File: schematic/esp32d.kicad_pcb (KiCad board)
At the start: 2 copper layers, 86.4 x 50.8 mm, 47 parts, among them IC1 CP2102N-A01-GQFN28R, J1 USB_B_Micro, J2 Conn_02x08_Odd_Even, J3 Conn_02x08_Odd_Even, J4 Conn_01x02, Q1 SS8050-G, Q2 SS8050-G, Q3 DMG2307L-7, SW1 SW_Push, U1 AMS1117-3.3, U2 ESP32-WROOM-32D, U3 DizzyBITLogo, U4 MCP73831-2-OT

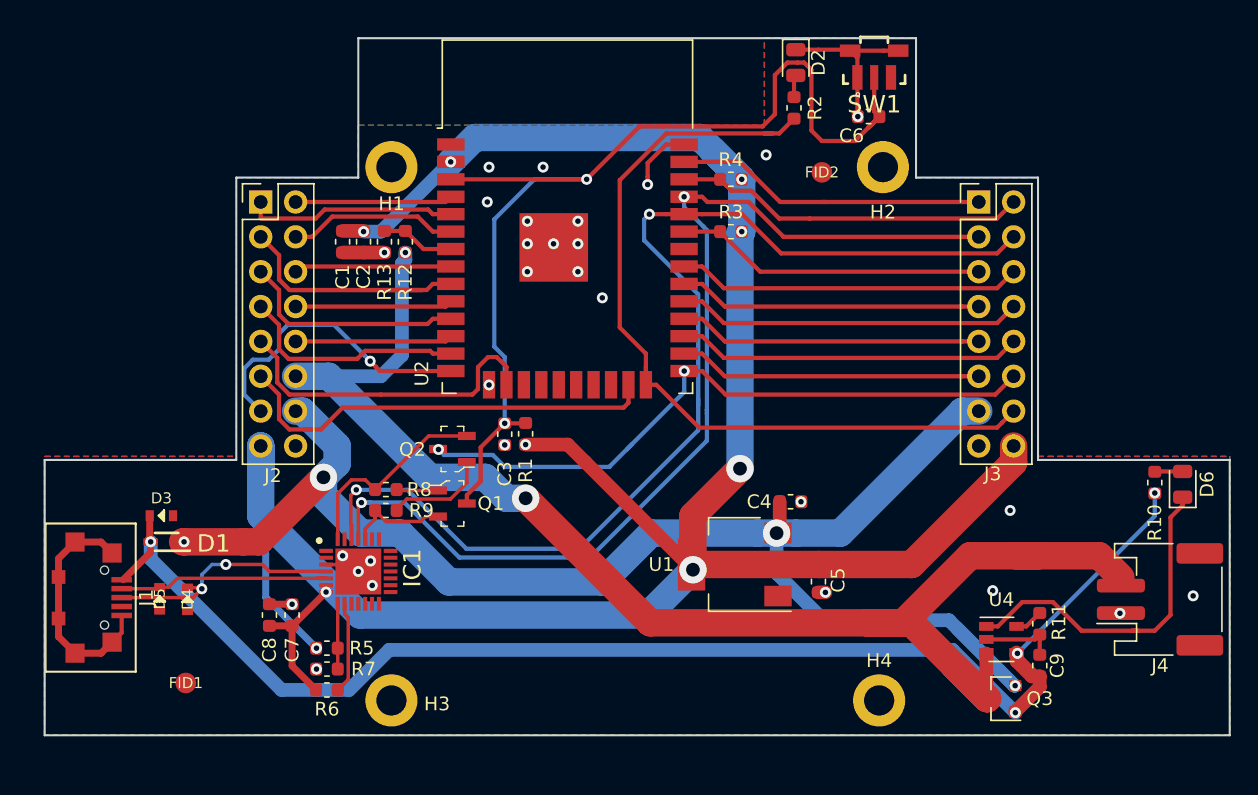
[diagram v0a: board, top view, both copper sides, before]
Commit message: Added Standard module design
Added Part numbers
Modified footprint positions to match standard module design
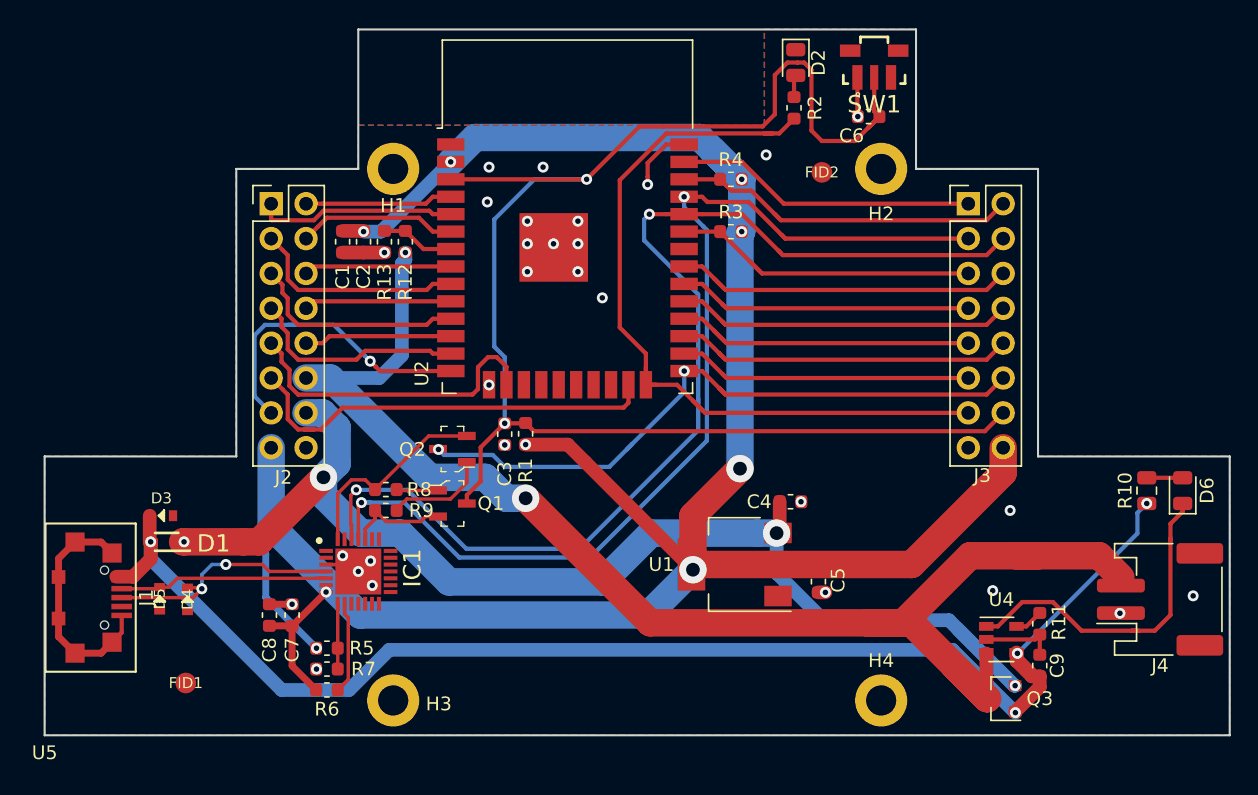
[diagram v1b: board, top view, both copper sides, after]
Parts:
- added U5: DizzyBIT-Layout, DizzyBit:DizzyBit-Din Rail Module, F.Cu at (76.2, 146.1)
- R10: footprint Capacitor_SMD:C_0603_1608Metric -> Resistor_SMD:R_0805_2012Metric
- moved R10 0.83 mm to (156.5, 128.2)
- moved J2 0.77 mm to (92.7, 107.3)
- moved J3 0.77 mm to (143.5, 107.3)
- moved D6 0.46 mm to (159.1, 128.2)
- moved H2 0.18 mm to (137.2, 104.8)
- moved H1 0.18 mm to (101.6, 104.8)
- moved H4 0.15 mm to (137.2, 143.5)
- moved H3 0.13 mm to (101.6, 143.5)
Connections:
- J3 pad 13: EXT_5V -> IO2
- J3 pad 14: IO2 -> EN
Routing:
- net EN: track 78.5 -> 114.1 mm
- net EXT_5V: track 122.5 -> 104.1 mm
- net IO33: track 34.0 -> 15.9 mm
- net GND: track 48.0 -> 38.3 mm
- net +3.3V: track 165.2 -> 161.0 mm
- net IO2: track 60.7 -> 58.3 mm
- net VBAT: track 106.3 -> 104.3 mm
- net VSPI_MOSI: track 22.9 -> 22.0 mm
- net HSPI_MOSI: track 24.2 -> 23.4 mm
- net IO15: track 32.3 -> 31.4 mm
- net I39: track 15.4 -> 14.7 mm
- net I34: track 12.4 -> 11.6 mm
- net IO26: track 16.6 -> 15.9 mm
- net HSPI_CLK: track 16.8 -> 16.0 mm
- net IO32: track 11.5 -> 10.8 mm
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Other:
- board size 86.4 x 50.8 mm -> 86.4 x 51.4 mm

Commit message: Optimized thermal dissipation
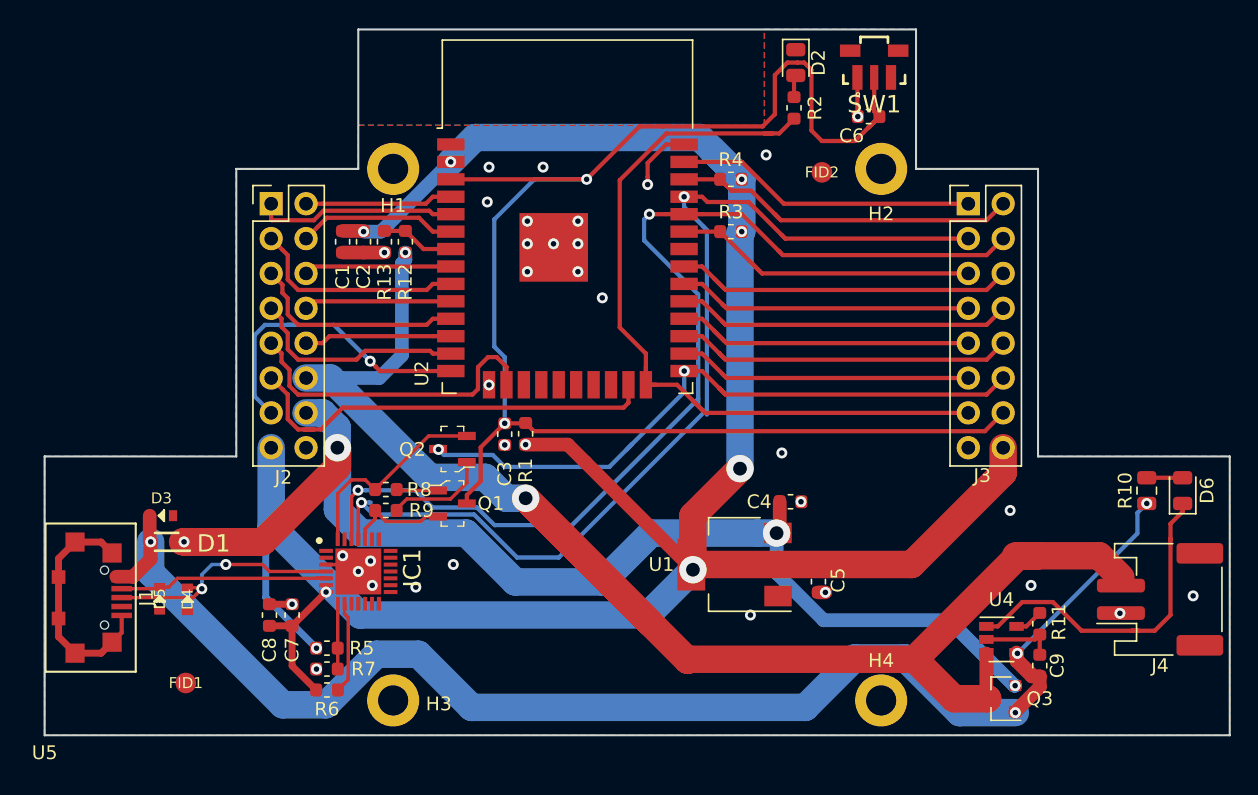
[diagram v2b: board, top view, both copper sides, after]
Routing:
- net EXT_5V: track 104.1 -> 112.6 mm
- net VBAT: track 104.3 -> 111.5 mm
- net VBUS: track 101.7 -> 105.9 mm
- net IO3: track 81.1 -> 78.2 mm
- net IO1: track 74.8 -> 73.5 mm
- net GND: vias 29 -> 33
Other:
- net class Default: clearance 0.1 -> 0.2
- rule trace_clearance: 0.1 -> 0.2

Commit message: Repositioned LEDs to match the standard module design
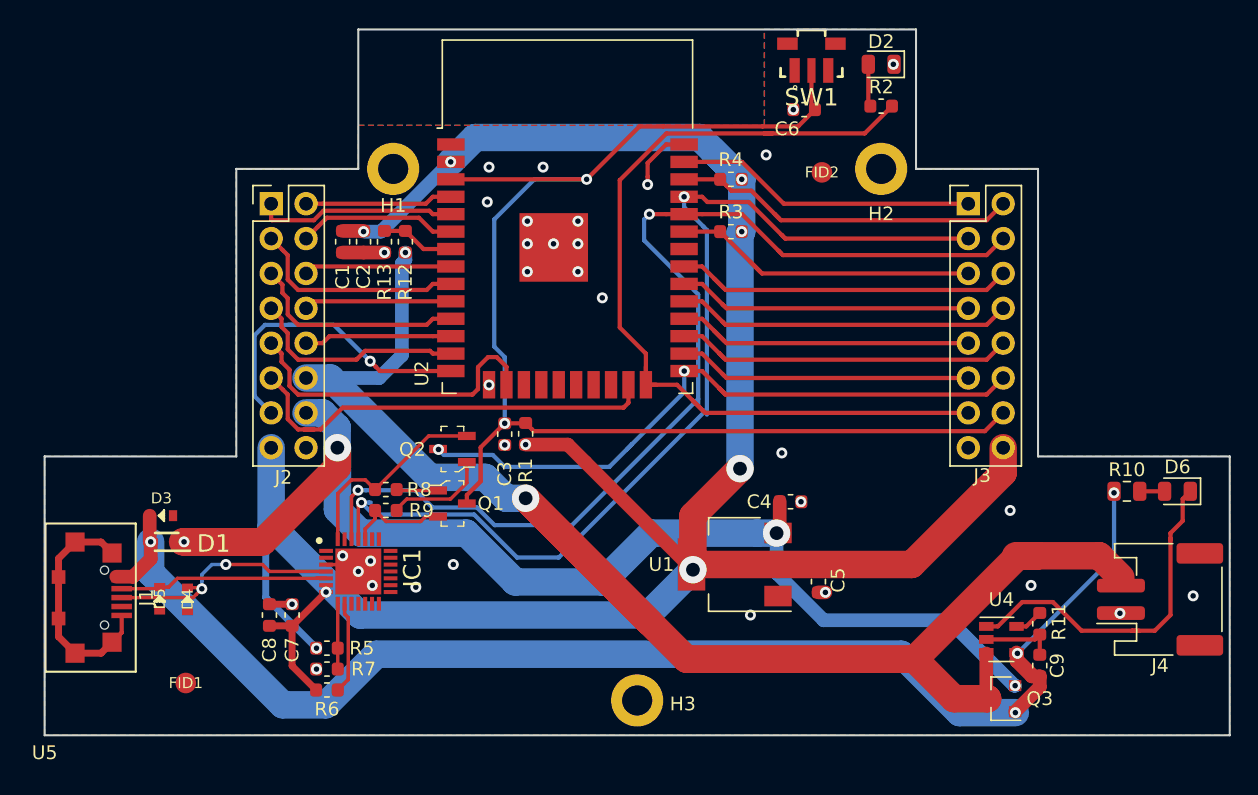
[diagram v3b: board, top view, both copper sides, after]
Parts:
- removed H4: MountingHole, MountingHole:MountingHole_2.2mm_M2_DIN965_Pad
- moved H3 17.8 mm to (119.4, 143.5)
- moved R2 6.35 mm to (137.2, 100.2), turned to 180 degrees
- moved D2 6.22 mm to (137.2, 97.2), turned to 180 degrees
- moved C6 4.73 mm to (131.5, 100.5)
- moved SW1 4.60 mm to (132.1, 95.5)
- moved R10 1.45 mm to (155.1, 128.3), turned to 180 degrees
- moved D6 0.38 mm to (158.8, 128.3), turned to 180 degrees
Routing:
- net VBAT: track 111.5 -> 127.9 mm
- net EN: track 114.1 -> 99.4 mm
- net IO2: track 58.3 -> 65.9 mm
- net VBUS: track 105.9 -> 102.7 mm
- net GND: track 38.3 -> 35.6 mm, vias 33 -> 34
- net Net-(D2-Pad2): track 1.63 -> 3.11 mm
- net Net-(D6-Pad1): track 25.0 -> 26.1 mm
- net Net-(D6-Pad2): track 2.62 -> 1.81 mm
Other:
- board text added: "ESP32D MCU"

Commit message: Changed 3.3V position for better PCB exposure
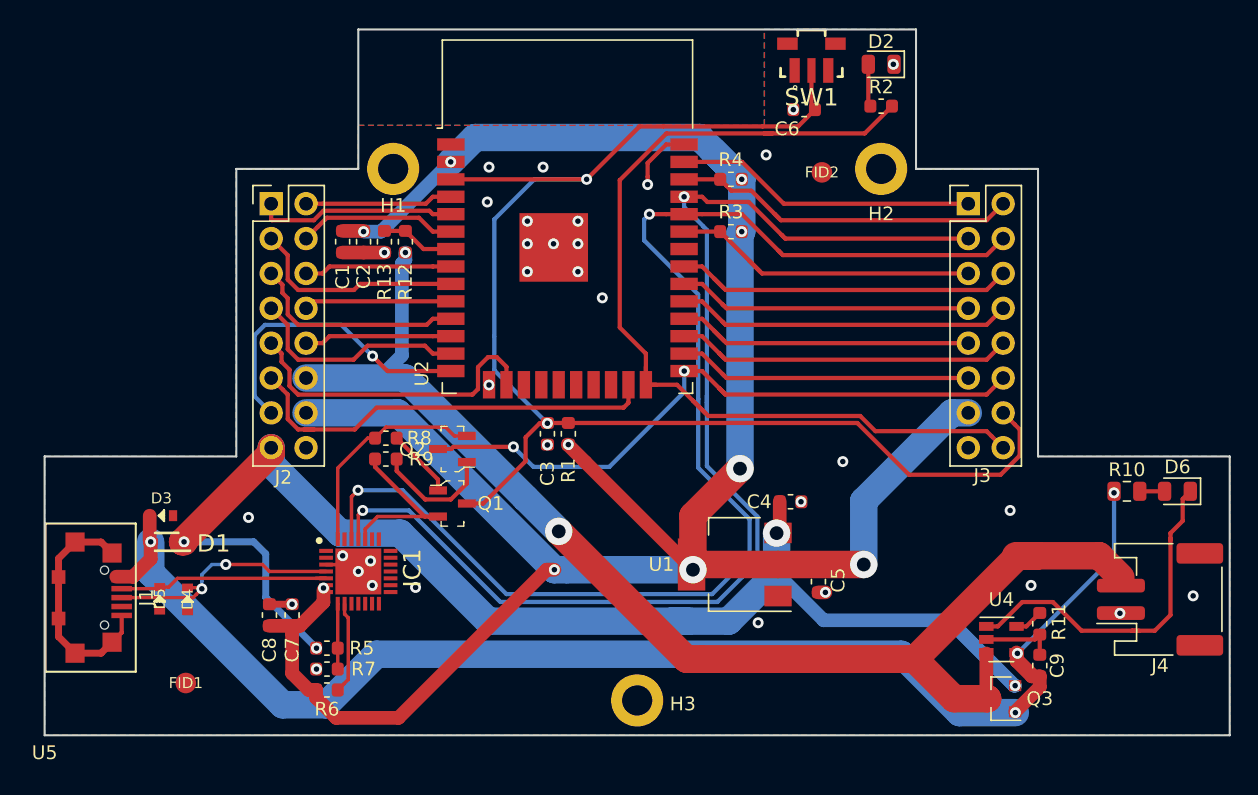
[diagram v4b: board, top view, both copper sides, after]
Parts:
- moved R8 3.75 mm to (101.1, 124.4)
- moved R9 3.75 mm to (101.1, 125.9)
- moved C3 3.11 mm to (112.8, 124.1)
- moved R1 3.11 mm to (114.4, 124.1)
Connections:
- J2 pad 14: EXT_5V -> +3.3V
- J2 pad 15: +3.3V -> EXT_5V
- J3 pad 13: IO2 -> +3.3V
- J3 pad 16: +3.3V -> IO2
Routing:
- net IO1: track 73.5 -> 92.0 mm
- net IO3: track 78.2 -> 94.4 mm
- net VBAT: track 127.9 -> 115.0 mm
- net +3.3V: track 161.0 -> 173.8 mm, vias 8 -> 10
- net EXT_5V: track 112.6 -> 101.7 mm, vias 5 -> 4
- net EN: track 99.4 -> 105.8 mm
- net RTS: track 7.46 -> 13.1 mm
- net IO2: track 65.9 -> 69.6 mm
- net Net-(Q1-Pad1): track 3.13 -> 5.15 mm
- net Net-(Q2-Pad1): track 7.56 -> 8.88 mm
- net DTR: track 15.1 -> 16.1 mm
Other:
- net class Default: clearance 0.2 -> 0.1
- rule trace_clearance: 0.2 -> 0.1

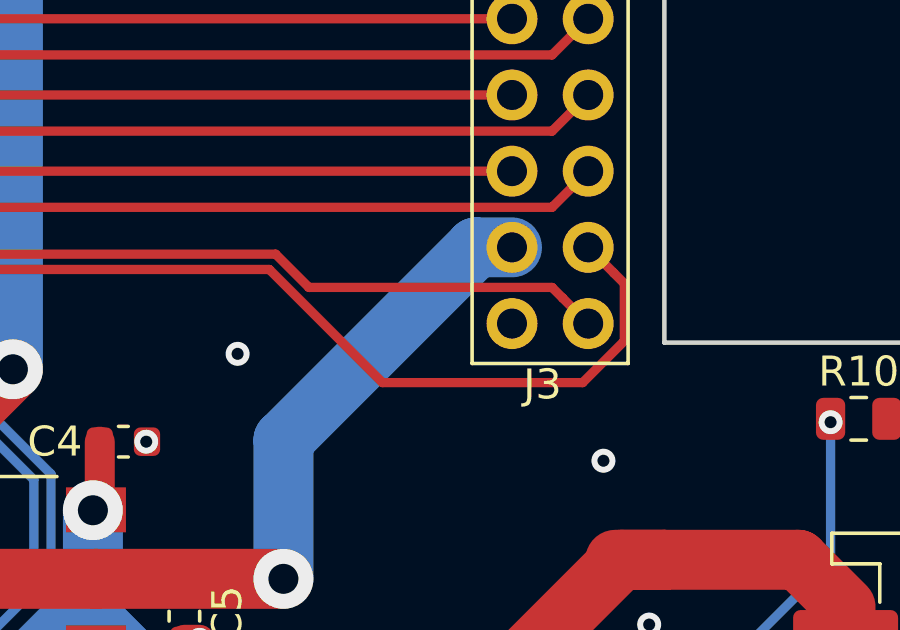
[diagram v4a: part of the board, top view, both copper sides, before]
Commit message: Changed EN and IO2 position
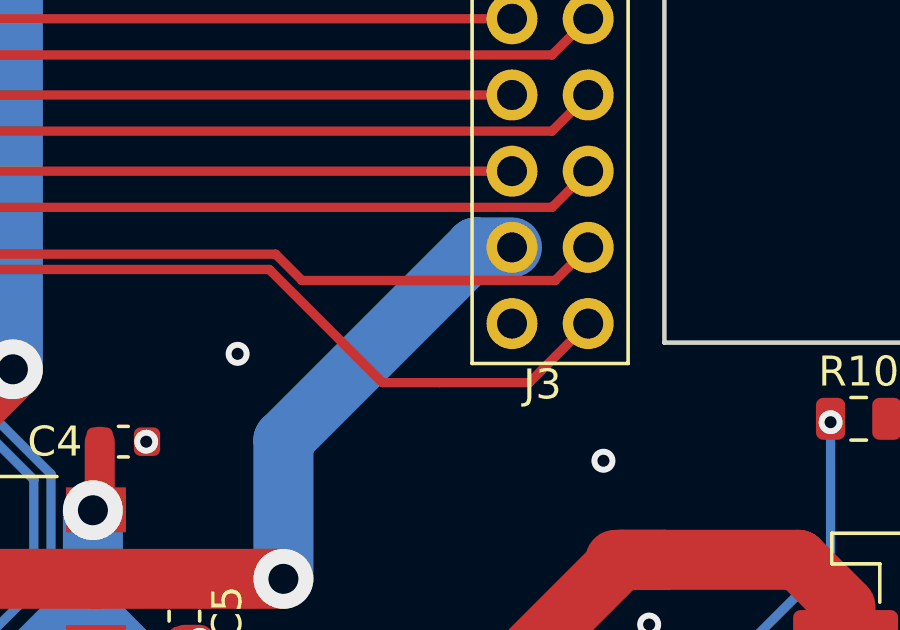
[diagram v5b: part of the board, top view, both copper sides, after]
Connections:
- J3 pad 14: EN -> IO2
- J3 pad 16: IO2 -> EN
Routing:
- net EN: track 105.8 -> 101.2 mm
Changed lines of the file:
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@@
     (thickness 1.6)
     (drawings 13)
-    (tracks 526)
+    (tracks 523)
     (zones 0)
     (modules 47)
@@
       (net 26 +3.3V))
     (pad 14 thru_hole oval (at 2.54 15.24) (size 1.7 1.7) (drill 1) (layers *.Cu *.Mask)
+      (net 12 IO2))
+    (pad 15 thru_hole oval (at 0 17.78) (size 1.7 1.7) (drill 1) (layers *.Cu *.Mask)
+      (net 1 GND))
+    (pad 16 thru_hole oval (at 2.54 17.78) (size 1.7 1.7) (drill 1) (layers *.Cu *.Mask)
       (net 2 EN))
-    (pad 15 thru_hole oval (at 0 17.78) (size 1.7 1.7) (drill 1) (layers *.Cu *.Mask)
-      (net 1 GND))
-    (pad 16 thru_hole oval (at 2.54 17.78) (size 1.7 1.7) (drill 1) (layers *.Cu *.Mask)
-      (net 12 IO2))
     (model ${KISYS3DMOD}/Connector_PinHeader_2.54mm.3dshapes/PinHeader_2x08_P2.54mm_Vertical.wrl
       (at (xyz 0 0 0))
@@
   (segment (start 111.252 124.338815) (end 111.252 126.070264) (width 0.31) (layer F.Cu) (net 2))
   (segment (start 108.163264 129.159) (end 108.585 128.737264) (width 0.31) (layer F.Cu) (net 2))
-  (segment (start 146.899999 123.404999) (end 146.05 122.555) (width 0.31) (layer F.Cu) (net 2))
-  (segment (start 145.864902 127.0635) (end 147.255001 125.673401) (width 0.31) (layer F.Cu) (net 2))
-  (segment (start 147.255001 125.673401) (end 147.255001 123.760001) (width 0.31) (layer F.Cu) (net 2))
-  (segment (start 139.192 127.0635) (end 145.864902 127.0635) (width 0.31) (layer F.Cu) (net 2))
   (segment (start 114.3635 123.2915) (end 135.42 123.2915) (width 0.31) (layer F.Cu) (net 2))
   (segment (start 135.42 123.2915) (end 139.192 127.0635) (width 0.31) (layer F.Cu) (net 2))
-  (segment (start 147.255001 123.760001) (end 146.899999 123.404999) (width 0.31) (layer F.Cu) (net 2))
+  (segment (start 144.0815 127.0635) (end 141.097 127.0635) (width 0.31) (layer F.Cu) (net 2))
+  (segment (start 146.05 125.095) (end 144.0815 127.0635) (width 0.31) (layer F.Cu) (net 2))
+  (segment (start 139.192 127.0635) (end 141.097 127.0635) (width 0.31) (layer F.Cu) (net 2))
   (segment (start 104.49 111.887) (end 105.8 111.887) (width 0.31) (layer F.Cu) (net 3))
   (segment (start 96.960081 111.887) (end 104.49 111.887) (width 0.31) (layer F.Cu) (net 3))
@@
   (segment (start 135.958501 102.191999) (end 137.9475 100.203) (width 0.31) (layer F.Cu) (net 12))
   (segment (start 128.651 102.191999) (end 135.958501 102.191999) (width 0.31) (layer F.Cu) (net 12))
-  (segment (start 135.631254 122.78149) (end 136.739763 123.889999) (width 0.31) (layer F.Cu) (net 12))
-  (segment (start 144.844999 123.889999) (end 145.200001 124.245001) (width 0.31) (layer F.Cu) (net 12))
-  (segment (start 136.739763 123.889999) (end 144.844999 123.889999) (width 0.31) (layer F.Cu) (net 12))
   (segment (start 124.55949 122.78149) (end 135.631254 122.78149) (width 0.31) (layer F.Cu) (net 12))
   (segment (start 123.444 121.666) (end 124.55949 122.78149) (width 0.31) (layer F.Cu) (net 12))
-  (segment (start 145.200001 124.245001) (end 146.05 125.095) (width 0.31) (layer F.Cu) (net 12))
+  (segment (start 136.509765 123.660001) (end 135.631254 122.78149) (width 0.31) (layer F.Cu) (net 12))
+  (segment (start 144.944999 123.660001) (end 136.509765 123.660001) (width 0.31) (layer F.Cu) (net 12))
+  (segment (start 146.05 122.555) (end 144.944999 123.660001) (width 0.31) (layer F.Cu) (net 12))
   (segment (start 124.11 119.507) (end 122.809 119.507) (width 0.31) (layer F.Cu) (net 13))
   (segment (start 122.809 119.507) (end 122.8 119.507) (width 0.31) (layer F.Cu) (net 13))
